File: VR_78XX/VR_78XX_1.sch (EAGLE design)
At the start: 23 parts, among them U1 7809

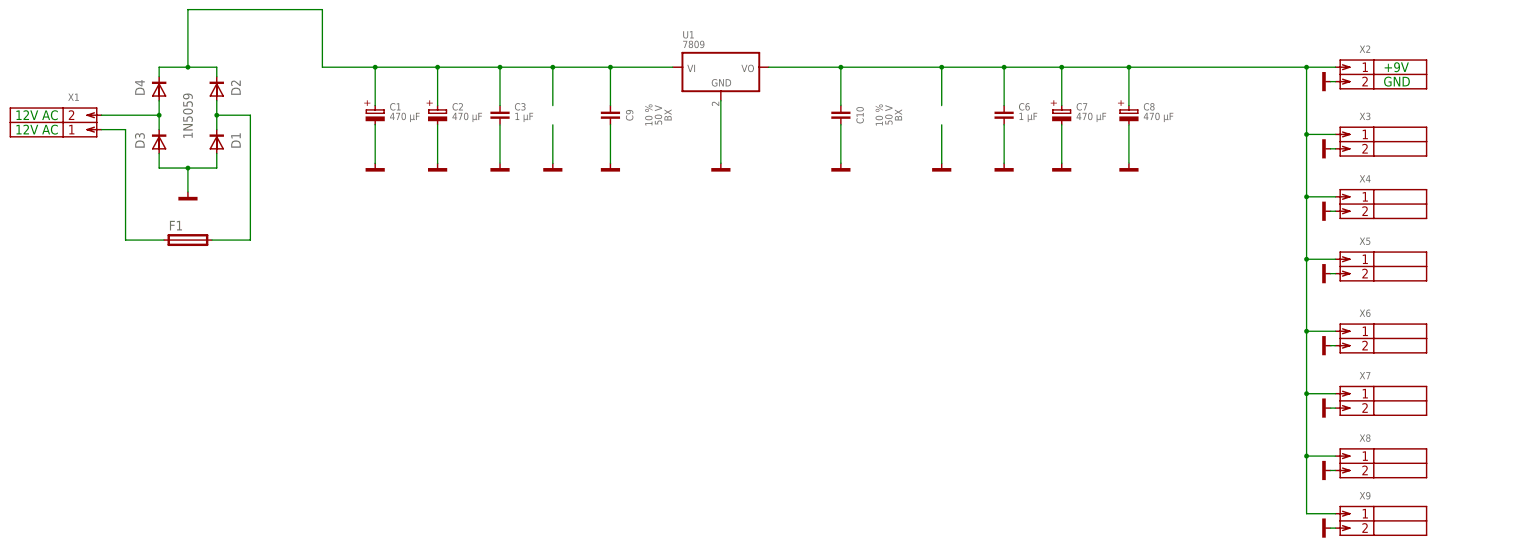
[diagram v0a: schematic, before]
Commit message: layout, caps
cleaned layout a little bit, added ceramic bypass caps.
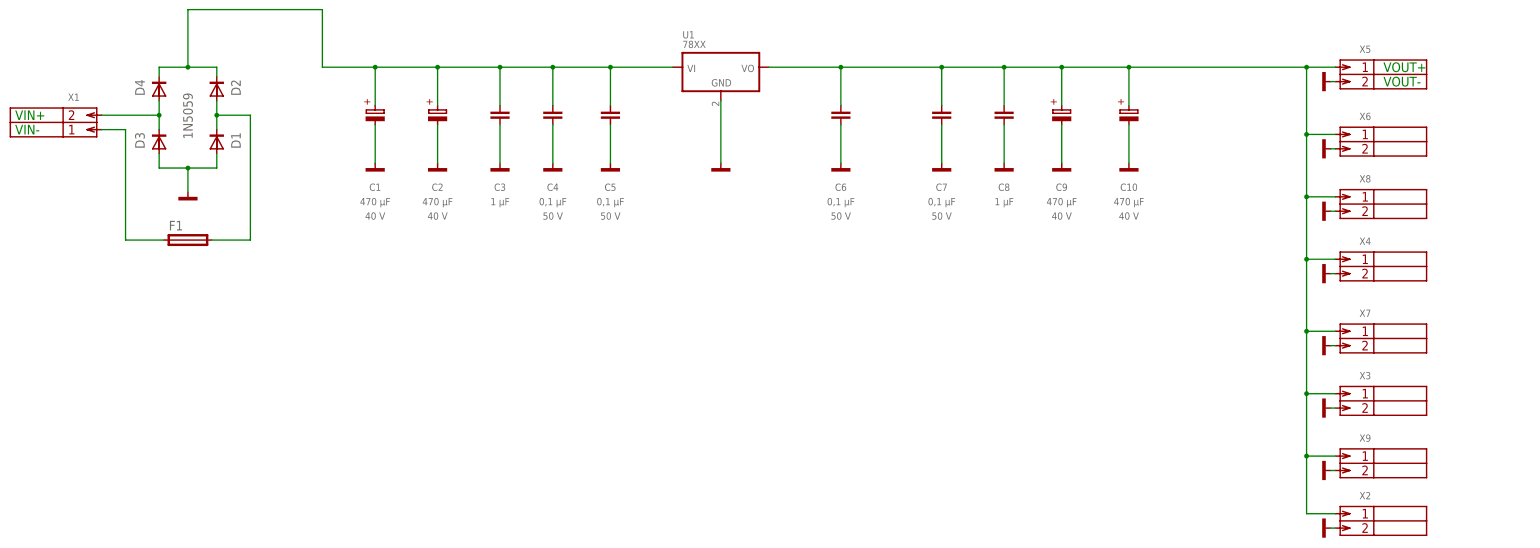
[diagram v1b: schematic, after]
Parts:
- added C4, C5: 0,1 µF, rcl_a:C-EU050-025X075
- C1, C2: device cap_vishay-pol_a:BEYSHLAG-118AHT0 -> cap_vishay-pol_a:BEYSHLAG-118/119AHTC; VOLTAGE (none) -> 40 V
- C10, C9: value (none) -> 470 µF; device rcl_a:C-EU050-025X075 -> cap_vishay-pol_a:BEYSHLAG-118/119AHTC; VOLTAGE (none) -> 40 V
- C6: value 1 µF -> 0,1 µF; device CDE_DMM:1 -> rcl_a:C-EU050-025X075
- C7: value 470 µF -> 0,1 µF; device cap_vishay-pol_a:BEYSHLAG-118AHT0 -> rcl_a:C-EU050-025X075
- C8: value 470 µF -> 1 µF; device cap_vishay-pol_a:BEYSHLAG-118AHT0 -> CDE_DMM:1
- U1: value 7809 -> 78XX
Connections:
- net +5V: now also C10.+, C7.1, C8.1, C9.+; no longer C10.1, C7.+, C8.+
- net GND: now also C10.-, C4.2, C5.2, C7.2, C8.2, C9.-; no longer C10.2, C7.-, C8.-, C9.2
- net VDD2: now also C4.1, C5.1; no longer C9.1
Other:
- note added: "VIN+"
- note added: "VIN-"
- note added: "VOUT+"
- note added: "VOUT-"
- note removed: "+9V"
- note removed: "12V AC"
- note removed: "GND"
- moved on the sheet: X2, X3, X4, X5, X6, X7, X8, X9

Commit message: added more decoupling caps
Added more decoupling caps
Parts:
- added C11: 1 µF, rcl_a:C-EU050-025X075
- added C12: 1 µF, CDE_DMM:1
- added C13, C14: 470 µF, cap_vishay-pol_a:BEYSHLAG-118/119AHTC
- C10: value 470 µF -> 1 µF; device cap_vishay-pol_a:BEYSHLAG-118/119AHTC -> rcl_a:C-EU050-025X075; VOLTAGE 40 V -> (none)
- C4, C5: value 0,1 µF -> 1 µF
- C8: value 1 µF -> 0,1 µF; device CDE_DMM:1 -> rcl_a:C-EU050-025X075
- C9: value 470 µF -> 0,1 µF; device cap_vishay-pol_a:BEYSHLAG-118/119AHTC -> rcl_a:C-EU050-025X075; VOLTAGE 40 V -> (none)
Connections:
- removed net +5V: C10.+, C6.1, C7.1, C8.1, C9.+, U1.VO, X2.1, X3.1, X4.1, X5.1, X6.1, X7.1, X8.1, X9.1
- removed net VDD2: C1.+, C2.+, C3.1, C4.1, C5.1, D2.C, D4.C, U1.VI
- new net VIN+: C1.+, C2.+, C3.1, C4.1, C5.1, C6.1, C7.1, D2.C, D4.C, U1.VI
- new net VOUT+: C10.1, C11.1, C12.1, C13.+, C14.+, C8.1, C9.1, U1.VO, X2.1, X3.1, X4.1, X5.1, X6.1, X7.1, X8.1, X9.1
- net GND: now also C10.2, C11.2, C12.2, C13.-, C14.-, C9.2; no longer C10.-, C9.-
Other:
- moved on the sheet: C6, C7, U1, X2, X3, X4, X5, X6, X7, X8, X9
